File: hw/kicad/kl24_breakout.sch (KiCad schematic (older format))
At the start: 1 part

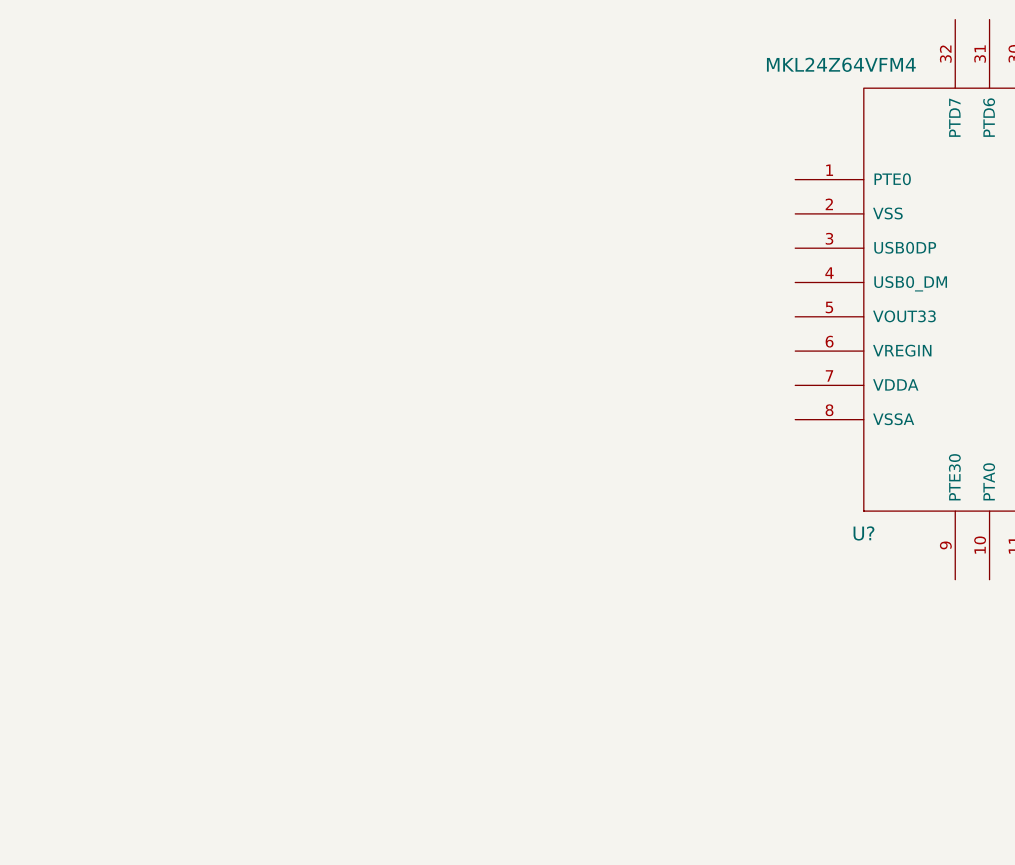
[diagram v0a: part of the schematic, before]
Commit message: - reference for 3.3/5v reg, add labels for some modules
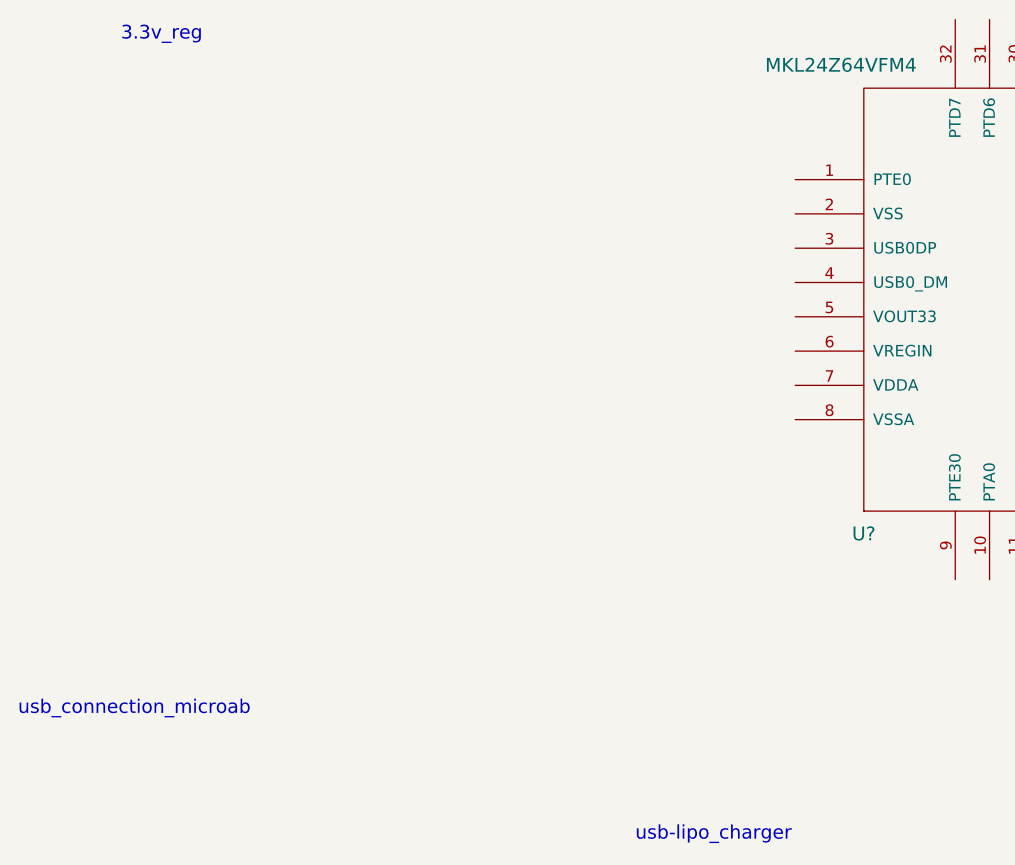
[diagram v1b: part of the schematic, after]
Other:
- note added: "3.3v_reg"
- note added: "usb-lipo_charger"
- note added: "usb_connection_microab"
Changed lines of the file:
@@
-EESchema Schematic File Version 2  date 2/28/2013 12:22:36 PM
+EESchema Schematic File Version 2  date 3/1/2013 12:53:30 PM
 LIBS:power
 LIBS:device
@@
 LIBS:valves
 LIBS:kl24_breakout
-EELAYER 43  0
+LIBS:kl24_breakout-cache
+EELAYER 25  0
 EELAYER END
 $Descr A4 11700 8267
@@
 Sheet 1 1
 Title ""
-Date "28 feb 2013"
+Date "1 mar 2013"
 Rev ""
 Comp ""
@@
 Comment4 ""
 $EndDescr
+Text Notes 4000 6200 0    60   ~ 0
+usb-lipo_charger
+Text Notes 1750 2700 0    60   ~ 0
+3.3v_reg
+Text Notes 1300 5650 0    60   ~ 0
+usb_connection_microab
 $Comp
 L MKL24Z64VFM4 U?

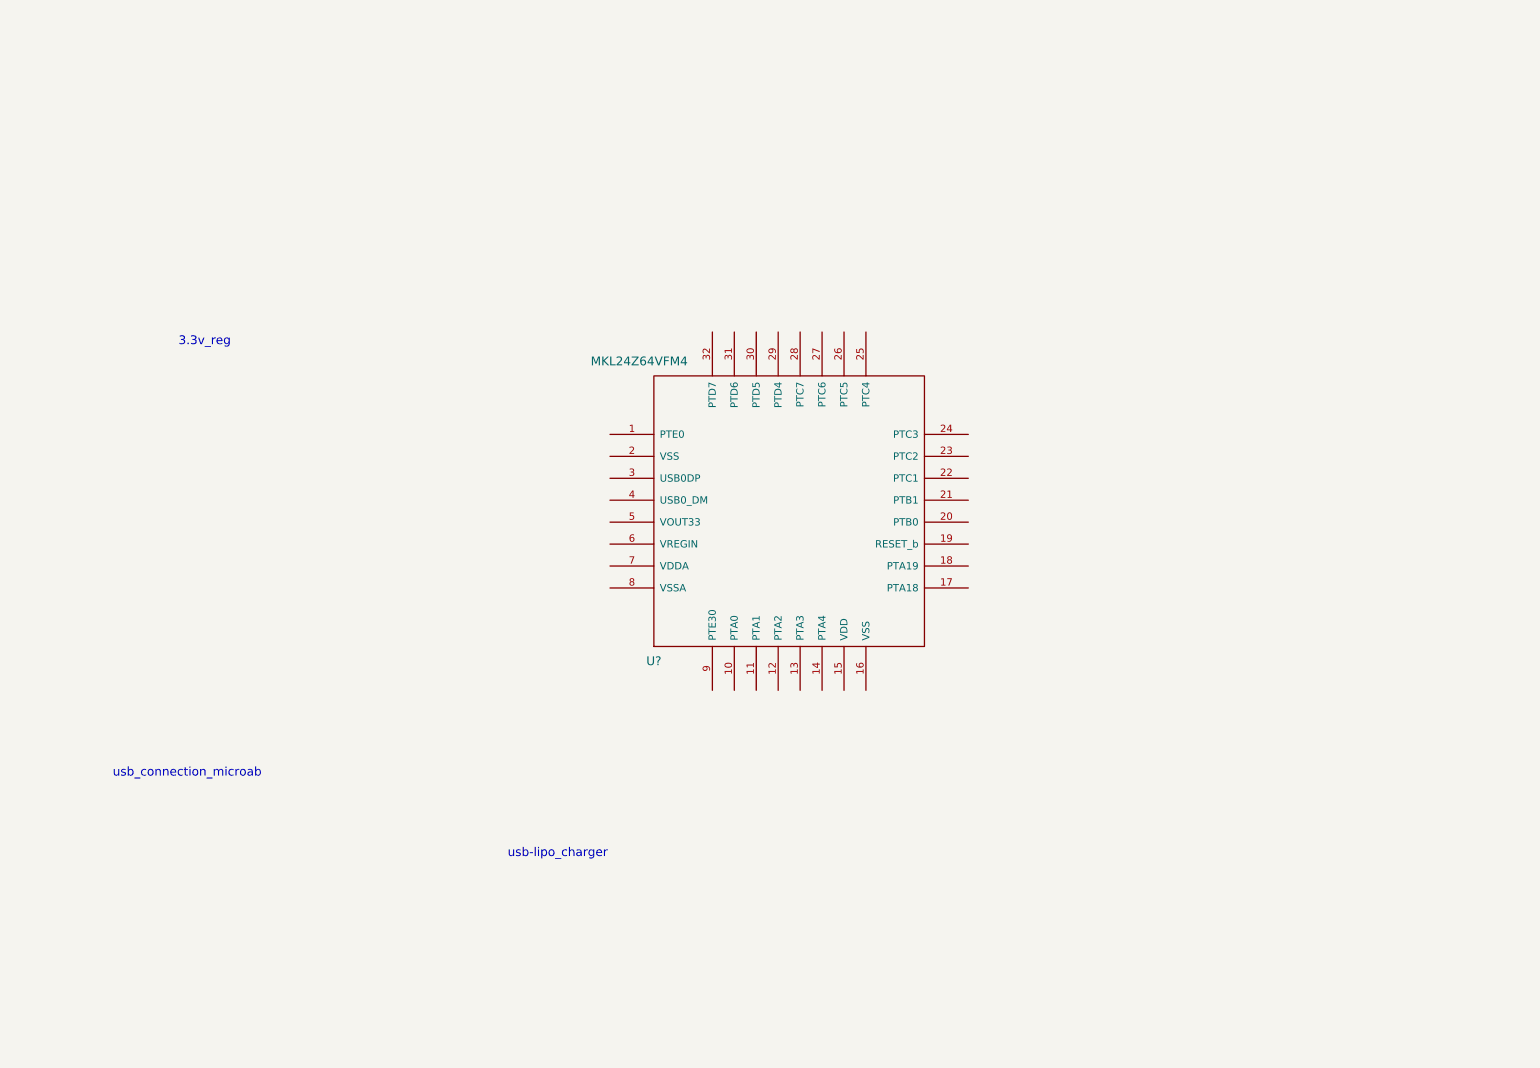
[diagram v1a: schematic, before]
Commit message: - add ref for 3.3 lin reg. add usb conn.
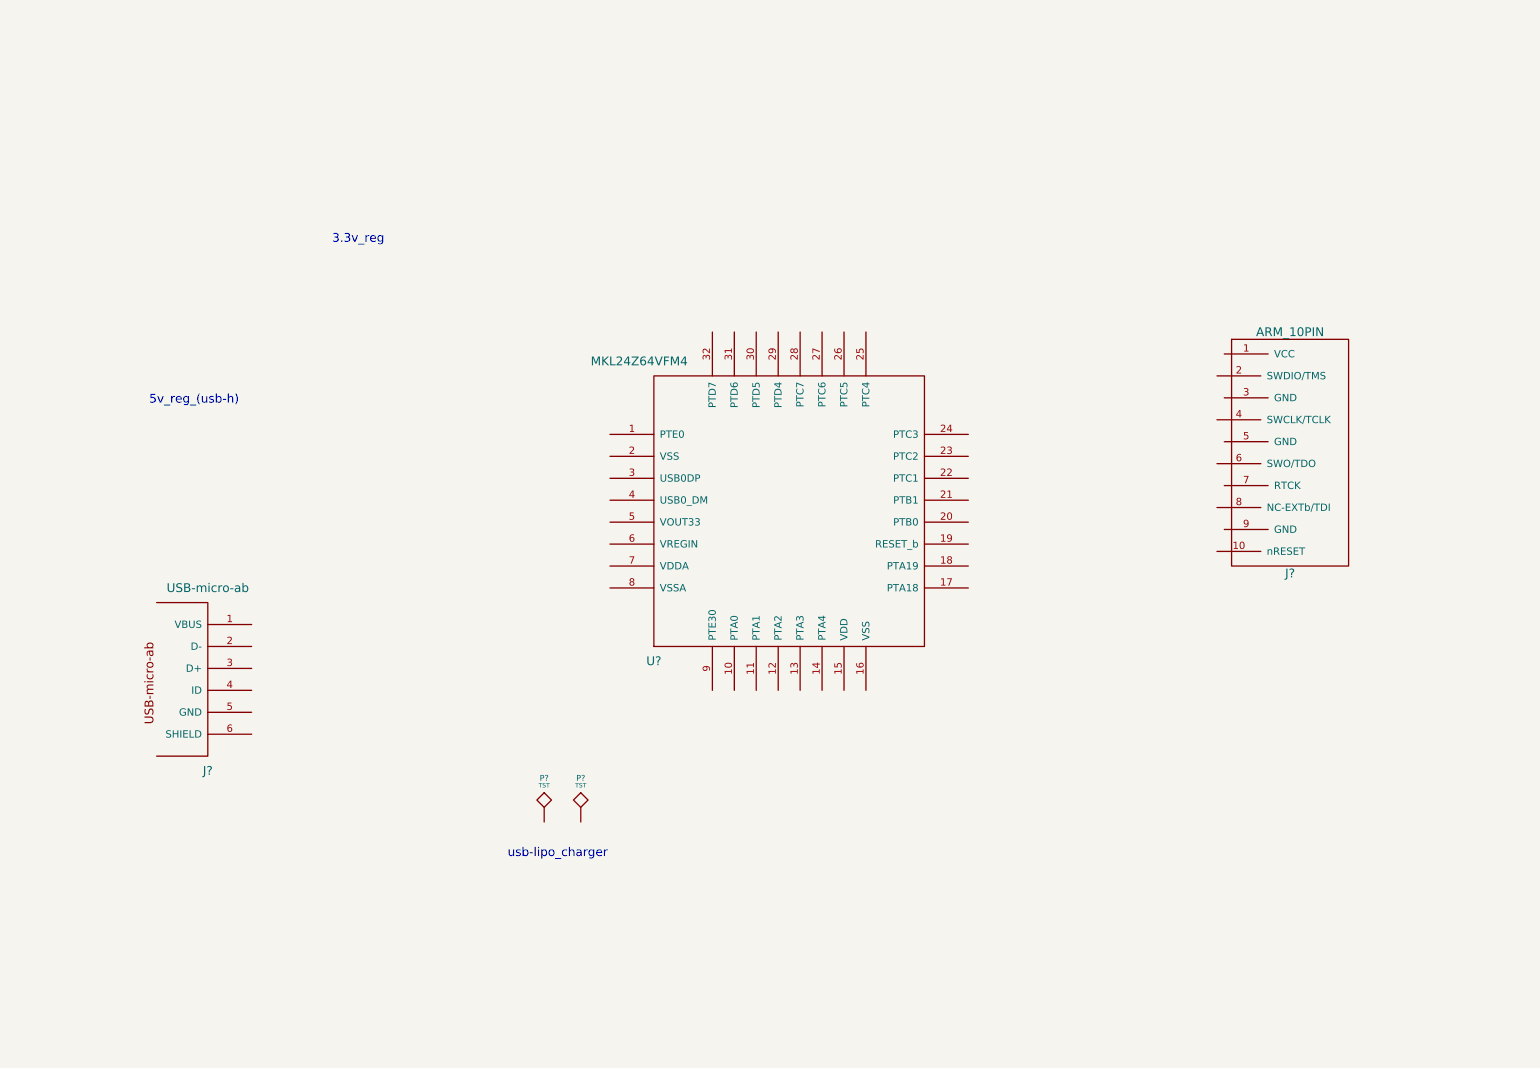
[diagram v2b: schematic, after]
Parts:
- added J?: USB-micro-ab, symbol USB-micro-ab
- added J?: ARM_10PIN, symbol ARM_10PIN
- added P? (x2): TST, symbol TST
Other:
- note added: "5v_reg_(usb-h)"
- note removed: "usb_connection_microab"
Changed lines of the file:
@@
-EESchema Schematic File Version 2  date 3/1/2013 12:53:30 PM
+EESchema Schematic File Version 2  date 3/4/2013 7:40:48 PM
 LIBS:power
 LIBS:device
@@
 Sheet 1 1
 Title ""
-Date "1 mar 2013"
+Date "5 mar 2013"
 Rev ""
 Comp ""
@@
 Comment4 ""
 $EndDescr
+$Comp
+L ARM_10PIN J?
+U 1 1 51353F09
+P 9350 3250
+F 0 "J?" H 9350 2250 60  0000 C CNN
+F 1 "ARM_10PIN" H 9350 3900 60  0000 C CNN
+	1    9350 3250
+	-1   0    0    -1
+$EndComp
+Text Notes 1550 3100 0    60   ~ 0
+5v_reg_(usb-h)
+$Comp
+L TST P?
+U 1 1 5135356E
+P 4500 5950
+F 0 "P?" H 4500 6250 40  0000 C CNN
+F 1 "TST" H 4500 6200 30  0000 C CNN
+	1    4500 5950
+	1    0    0    -1
+$EndComp
+$Comp
+L TST P?
+U 1 1 5135356A
+P 4250 5950
+F 0 "P?" H 4250 6250 40  0000 C CNN
+F 1 "TST" H 4250 6200 30  0000 C CNN
+	1    4250 5950
+	1    0    0    -1
+$EndComp
+$Comp
+L USB-micro-ab J?
+U 1 1 5135355A
+P 1950 5000
+F 0 "J?" H 1950 4400 60  0000 C CNN
+F 1 "USB-micro-ab" H 1950 5650 60  0000 C CNN
+	1    1950 5000
+	1    0    0    -1
+$EndComp
 Text Notes 4000 6200 0    60   ~ 0
 usb-lipo_charger
-Text Notes 1750 2700 0    60   ~ 0
+Text Notes 2800 2000 0    60   ~ 0
 3.3v_reg
-Text Notes 1300 5650 0    60   ~ 0
-usb_connection_microab
 $Comp
 L MKL24Z64VFM4 U?

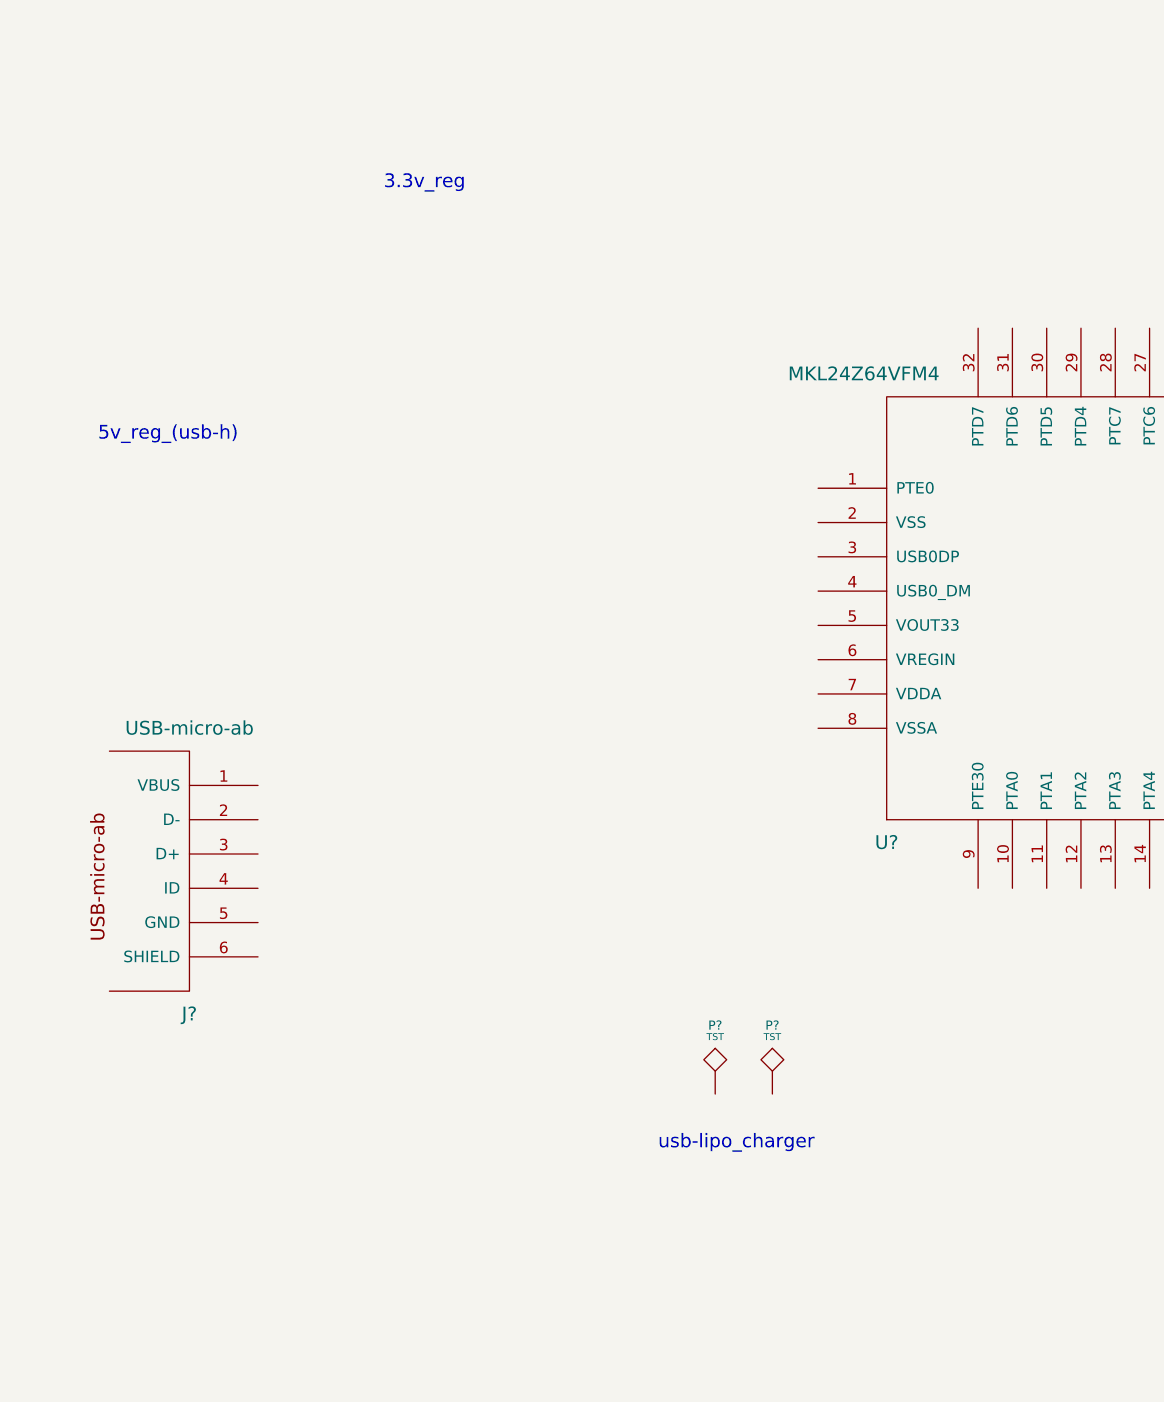
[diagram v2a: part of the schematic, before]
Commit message: - add the rest of the ic's
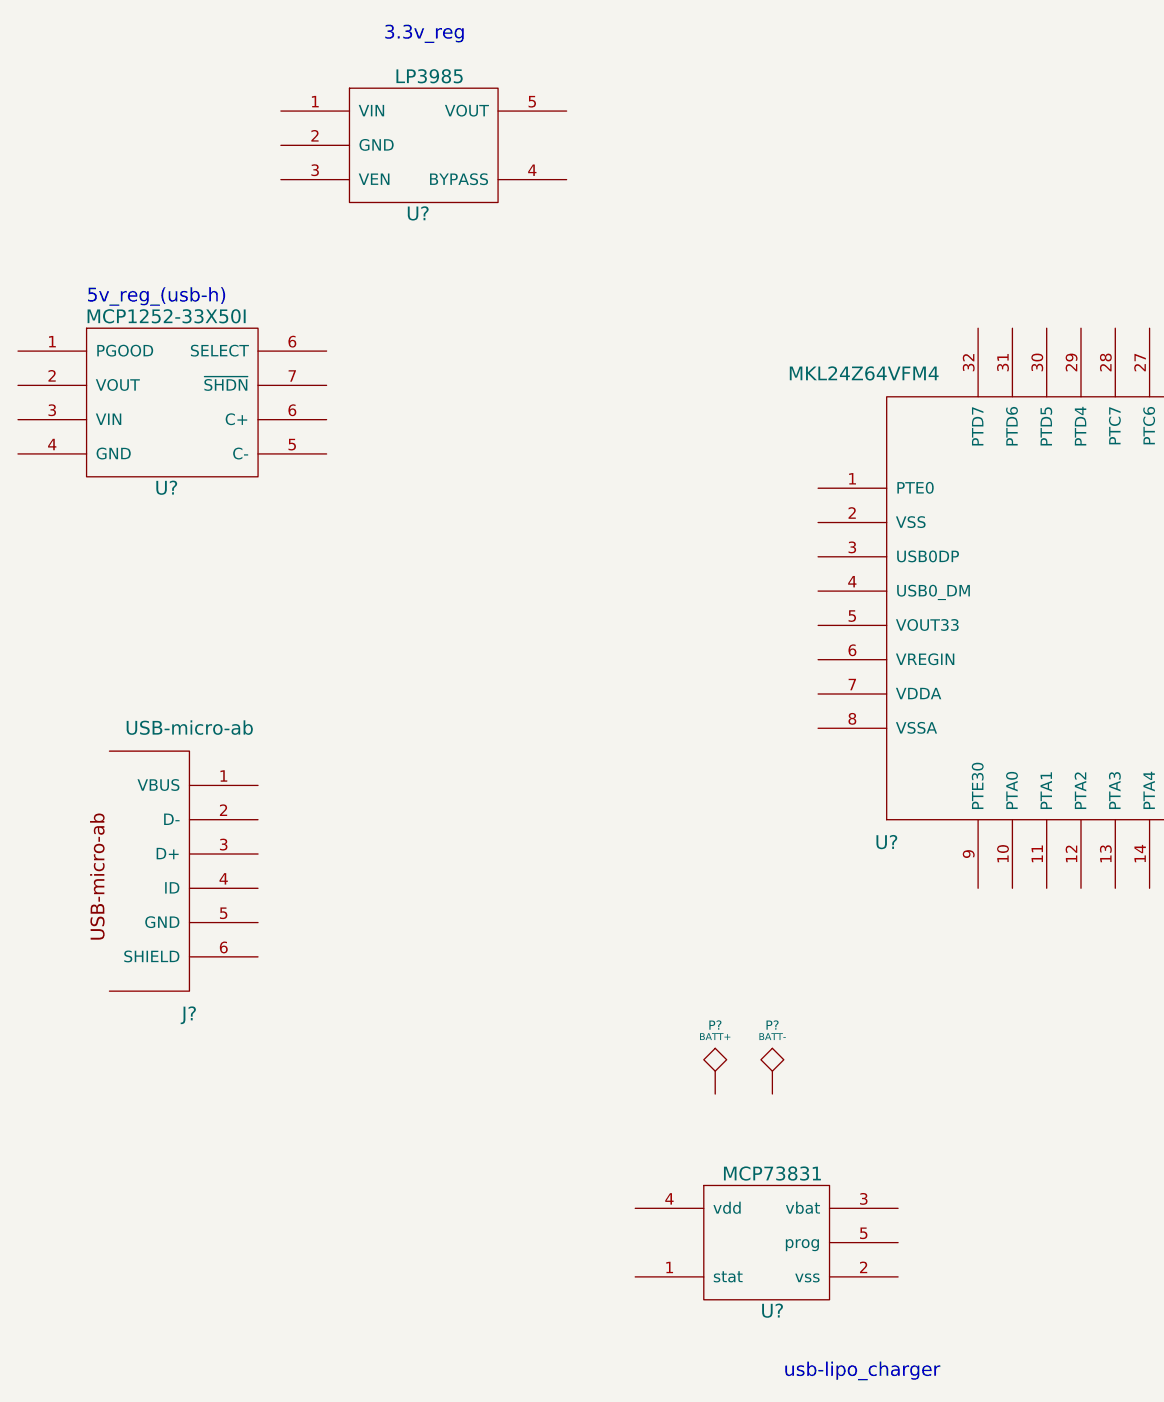
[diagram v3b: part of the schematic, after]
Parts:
- added U?: LP3985, symbol LP3985
- added U?: MCP1252-33X50I, symbol MCP1252-33X50I
- added U?: MCP73831, symbol MCP73831
- P?: value TST -> BATT+
- P?: value TST -> BATT-
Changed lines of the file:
@@
-EESchema Schematic File Version 2  date 3/4/2013 7:40:48 PM
+EESchema Schematic File Version 2  date 3/5/2013 1:18:51 PM
 LIBS:power
 LIBS:device
@@
 $EndDescr
 $Comp
+L MCP73831 U?
+U 1 1 513636F3
+P 4500 6600
+F 0 "U?" H 4500 6300 60  0000 C CNN
+F 1 "MCP73831" H 4500 6900 60  0000 C CNN
+	1    4500 6600
+	1    0    0    -1
+$EndComp
+$Comp
+L MCP1252-33X50I U?
+U 1 1 51363679
+P 1850 2950
+F 0 "U?" H 1850 2600 60  0000 C CNN
+F 1 "MCP1252-33X50I" H 1850 3350 60  0000 C CNN
+	1    1850 2950
+	1    0    0    -1
+$EndComp
+$Comp
+L LP3985 U?
+U 1 1 513635E4
+P 2950 1800
+F 0 "U?" H 2950 1500 60  0000 C CNN
+F 1 "LP3985" H 3000 2100 60  0000 C CNN
+	1    2950 1800
+	1    0    0    -1
+$EndComp
+$Comp
 L ARM_10PIN J?
 U 1 1 51353F09
@@
 	-1   0    0    -1
 $EndComp
-Text Notes 1550 3100 0    60   ~ 0
+Text Notes 1500 2500 0    60   ~ 0
 5v_reg_(usb-h)
 $Comp
@@
 P 4500 5950
 F 0 "P?" H 4500 6250 40  0000 C CNN
-F 1 "TST" H 4500 6200 30  0000 C CNN
+F 1 "BATT-" H 4500 6200 30  0000 C CNN
 	1    4500 5950
 	1    0    0    -1
@@
 P 4250 5950
 F 0 "P?" H 4250 6250 40  0000 C CNN
-F 1 "TST" H 4250 6200 30  0000 C CNN
+F 1 "BATT+" H 4250 6200 30  0000 C CNN
 	1    4250 5950
 	1    0    0    -1
@@
 	1    0    0    -1
 $EndComp
-Text Notes 4000 6200 0    60   ~ 0
+Text Notes 4550 7200 0    60   ~ 0
 usb-lipo_charger
-Text Notes 2800 2000 0    60   ~ 0
+Text Notes 2800 1350 0    60   ~ 0
 3.3v_reg
 $Comp
